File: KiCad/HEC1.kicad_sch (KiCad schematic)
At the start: 39 parts, among them J1 Barrel_Jack_Switch, J5 Screw_Terminal_01x02, U41 74LS02

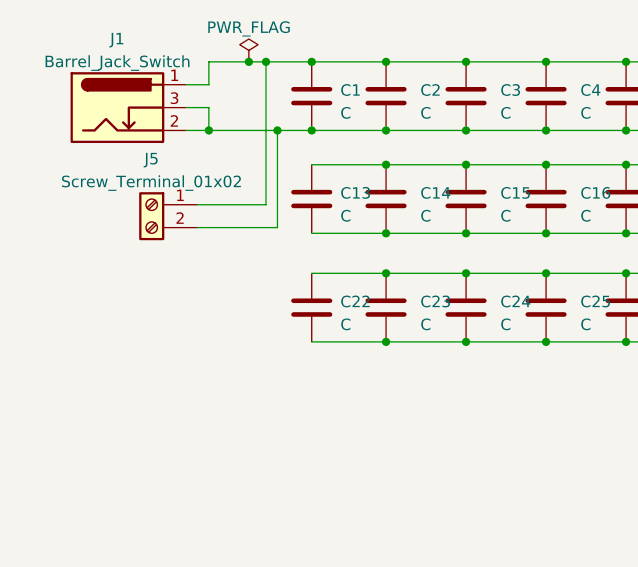
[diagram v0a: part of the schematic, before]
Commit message: More routing, a power LED
Did some easier routing. The current concern is that the already done easy routing would take up space for harder to route traces, making them even harder. However, one have to start somewhere... The power LED is added to assist debugging.
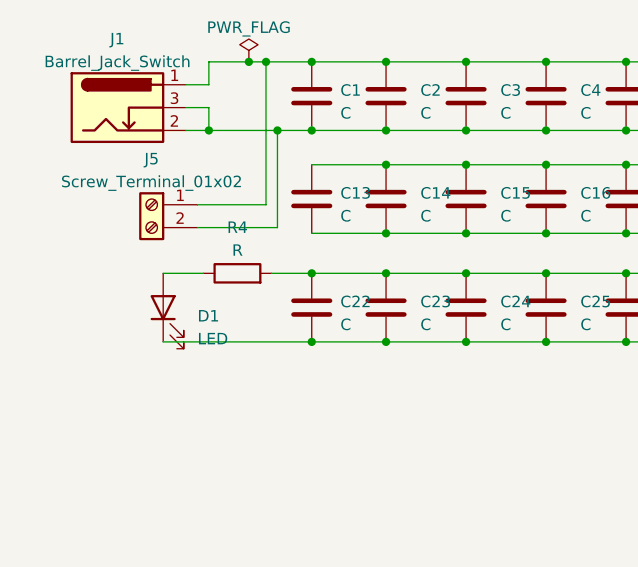
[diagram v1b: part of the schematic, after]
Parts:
- added D1: LED, LED_THT:LED_D3.0mm, symbol Device:LED
- added R4: R, Resistor_THT:R_Axial_DIN0207_L6.3mm_D2.5mm_P7.62mm_Horizontal, symbol Device:R
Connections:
- net GND: now also D1.1 (K)
- net VCC: now also R4.2
- new net: D1.2 (A), R4.1
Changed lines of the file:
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@@
   (junction (at 118.11 55.88) (diameter 0) (color 0 0 0 0)
   )
+  (junction (at 73.66 143.51) (diameter 0) (color 0 0 0 0)
+  )
   (junction (at 90.805 143.51) (diameter 0) (color 0 0 0 0)
   )
@@
   )
   (junction (at 177.165 28.575) (diameter 0) (color 0 0 0 0)
+  )
+  (junction (at 73.66 135.89) (diameter 0) (color 0 0 0 0)
   )
   (junction (at 68.58 112.395) (diameter 0) (color 0 0 0 0)
@@
     (stroke (width 0) (type default))
   )
+  (wire (pts (xy 57.15 135.89) (xy 61.595 135.89))
+    (stroke (width 0) (type default))
+  )
   (wire (pts (xy 133.985 60.96) (xy 133.985 43.815))
     (stroke (width 0) (type default))
@@
     (stroke (width 0) (type default))
   )
+  (wire (pts (xy 69.215 135.89) (xy 73.66 135.89))
+    (stroke (width 0) (type default))
+  )
   (wire (pts (xy 191.135 112.395) (xy 199.39 112.395))
     (stroke (width 0) (type default))
@@
   )
   (bus (pts (xy 113.03 83.185) (xy 118.11 83.185))
+    (stroke (width 0) (type default))
+  )
+  (wire (pts (xy 57.15 143.51) (xy 73.66 143.51))
     (stroke (width 0) (type default))
   )
@@
         (path "/87935374-b60a-4f41-99da-94b76103dd77"
           (reference "C27") (unit 1)
+        )
+      )
+    )
+  )
+  (symbol (lib_id "Device:LED") (at 57.15 139.7 90) (unit 1)
+    (in_bom yes) (on_board yes) (dnp no) (fields_autoplaced)
+    (property "Reference" "D1" (at 60.96 140.6525 90)
+      (effects (font (size 1.27 1.27)) (justify right))
+    )
+    (property "Value" "LED" (at 60.96 143.1925 90)
+      (effects (font (size 1.27 1.27)) (justify right))
+    )
+    (property "Footprint" "LED_THT:LED_D3.0mm" (at 57.15 139.7 0)
+      (effects (font (size 1.27 1.27)) hide)
+    )
+    (property "Datasheet" "~" (at 57.15 139.7 0)
+      (effects (font (size 1.27 1.27)) hide)
+    )
+    (pin "1")
+    (pin "2")
+    (instances
+      (project "HEC1"
+        (path "/87935374-b60a-4f41-99da-94b76103dd77"
+          (reference "D1") (unit 1)
         )
       )
@@
         )
       )
+    )
+  )
+  (symbol (lib_id "Device:R") (at 65.405 135.89 90) (unit 1)
+    (in_bom yes) (on_board yes) (dnp no) (fields_autoplaced)
+    (property "Reference" "R4" (at 65.405 130.81 90)
+      (effects (font (size 1.27 1.27)))
+    )
+    (property "Value" "R" (at 65.405 133.35 90)
+      (effects (font (size 1.27 1.27)))
+    )
+    (property "Footprint" "Resistor_THT:R_Axial_DIN0207_L6.3mm_D2.5mm_P7.62mm_Horizontal" (at 65.405 137.668 90)
+      (effects (font (size 1.27 1.27)) hide)
+    )
+    (property "Datasheet" "~" (at 65.405 135.89 0)
+      (effects (font (size 1.27 1.27)) hide)
+    )
+    (pin "1")
+    (pin "2")
+    (instances
+      (project "HEC1"
+        (path "/87935374-b60a-4f41-99da-94b76103dd77"
+          (reference "R4") (unit 1)
+        )
+      )

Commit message: Livestream commit
Committing live! Just to make sure that I don't lose 1 day of work.
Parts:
- removed unit 4 of U41
- removed unit 3 of U41
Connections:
- no-connect marks 3 -> 1

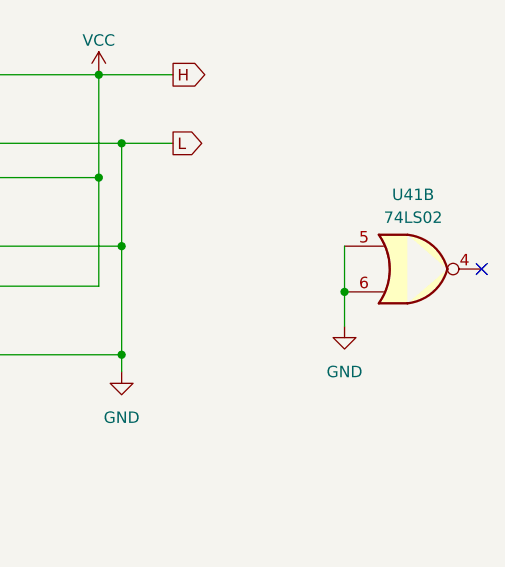
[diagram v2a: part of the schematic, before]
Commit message: Finish routing data bus
finished routing arguably the hardest part of the board: the data bus. The routing is mostly complete. However, the rest of traces are very hard to route. One more day of work is expected.
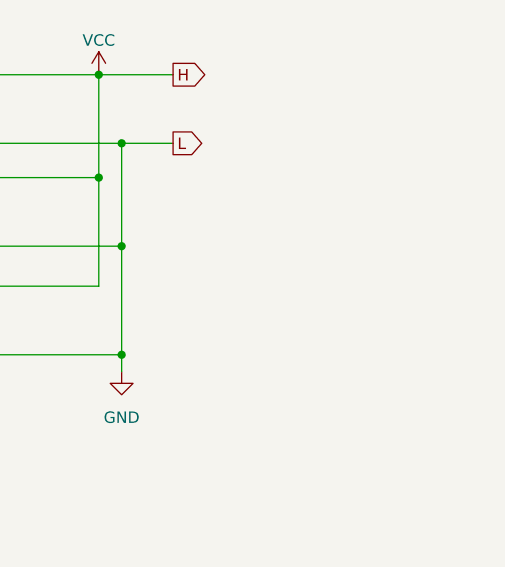
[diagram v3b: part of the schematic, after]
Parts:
- removed U41: 74LS02, Package_DIP:DIP-14_W7.62mm_Socket, symbol 74xx:74LS02
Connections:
- no-connect marks 1 -> 0
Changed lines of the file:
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@@
   (junction (at 193.675 120.015) (diameter 0) (color 0 0 0 0)
   )
-  (junction (at 218.44 136.525) (diameter 0) (color 0 0 0 0)
-  )
   (junction (at 144.145 123.825) (diameter 0) (color 0 0 0 0)
   )
@@
   (junction (at 161.29 120.015) (diameter 0) (color 0 0 0 0)
   )
-  (no_connect (at 233.68 133.985))
   (wire (pts (xy 90.805 112.395) (xy 99.695 112.395))
     (stroke (width 0) (type default))
@@
     (stroke (width 0) (type default))
   )
-  (wire (pts (xy 218.44 131.445) (xy 218.44 136.525))
-    (stroke (width 0) (type default))
-  )
   (wire (pts (xy 133.985 43.815) (xy 135.89 43.815))
     (stroke (width 0) (type default))
@@
   )
   (wire (pts (xy 144.145 131.445) (xy 161.29 131.445))
-    (stroke (width 0) (type default))
-  )
-  (wire (pts (xy 218.44 136.525) (xy 218.44 140.335))
     (stroke (width 0) (type default))
   )
@@
     )
   )
-  (symbol (lib_id "power:GND") (at 218.44 140.335 0) (unit 1)
-    (in_bom yes) (on_board yes) (dnp no) (fields_autoplaced)
-    (property "Reference" "#PWR0106" (at 218.44 146.685 0)
-      (effects (font (size 1.27 1.27)) hide)
-    )
-    (property "Value" "GND" (at 218.44 145.415 0)
-      (effects (font (size 1.27 1.27)))
-    )
-    (property "Footprint" "" (at 218.44 140.335 0)
-      (effects (font (size 1.27 1.27)) hide)
-    )
-    (property "Datasheet" "" (at 218.44 140.335 0)
-      (effects (font (size 1.27 1.27)) hide)
-    )
-    (pin "1")
-    (instances
-      (project "HEC1"
-        (path "/87935374-b60a-4f41-99da-94b76103dd77"
-          (reference "#PWR0106") (unit 1)
-        )
-      )
-    )
-  )
   (symbol (lib_id "power:GND") (at 193.675 145.415 0) (unit 1)
     (in_bom yes) (on_board yes) (dnp no) (fields_autoplaced)
@@
         )
       )
-    )
-  )
-  (symbol (lib_id "74xx:74LS02") (at 226.06 133.985 0) (unit 2)
-    (in_bom yes) (on_board yes) (dnp no) (fields_autoplaced)
-    (property "Reference" "U41" (at 226.06 125.73 0)
-      (effects (font (size 1.27 1.27)))
-    )
-    (property "Value" "74LS02" (at 226.06 128.27 0)
-      (effects (font (size 1.27 1.27)))
-    )
-    (property "Footprint" "Package_DIP:DIP-14_W7.62mm_Socket" (at 226.06 133.985 0)
-      (effects (font (size 1.27 1.27)) hide)
-    )
-    (property "Datasheet" "http://www.ti.com/lit/gpn/sn74ls02" (at 226.06 133.985 0)
-      (effects (font (size 1.27 1.27)) hide)
-    )
-    (pin "1")
-    (pin "2")
-    (pin "3")
-    (pin "4")
-    (pin "5")
-    (pin "6")
-    (pin "10")
-    (pin "8")
-    (pin "9")
-    (pin "11")
-    (pin "12")
-    (pin "13")
-    (pin "14")
-    (pin "7")
-    (instances
-      (project "HEC1"
-        (path "/87935374-b60a-4f41-99da-94b76103dd77/2930b625-d6a3-4a7f-9d41-a454efcef99d"
-          (reference "U41") (unit 2)
-        )
-        (path "/87935374-b60a-4f41-99da-94b76103dd77"
-          (reference "U41") (unit 2)
-        )
-      )

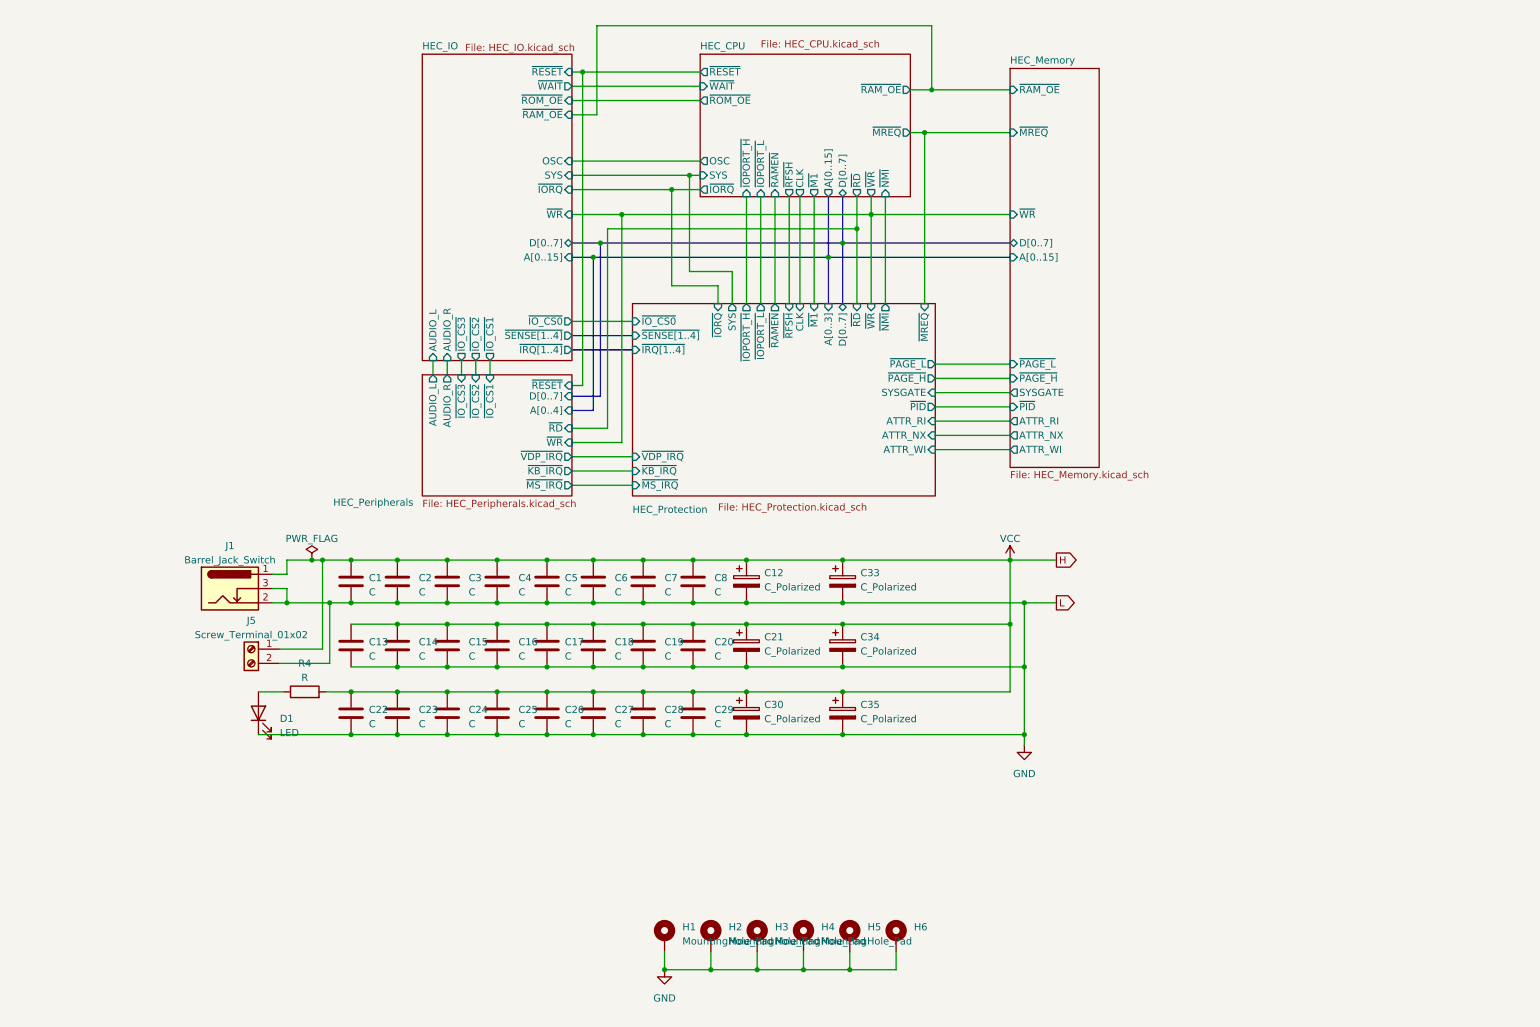
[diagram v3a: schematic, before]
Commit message: Change LED display type
Changed LED display to include two decimal points to indicate usr/sys mode. This type of LED display is easier to source.
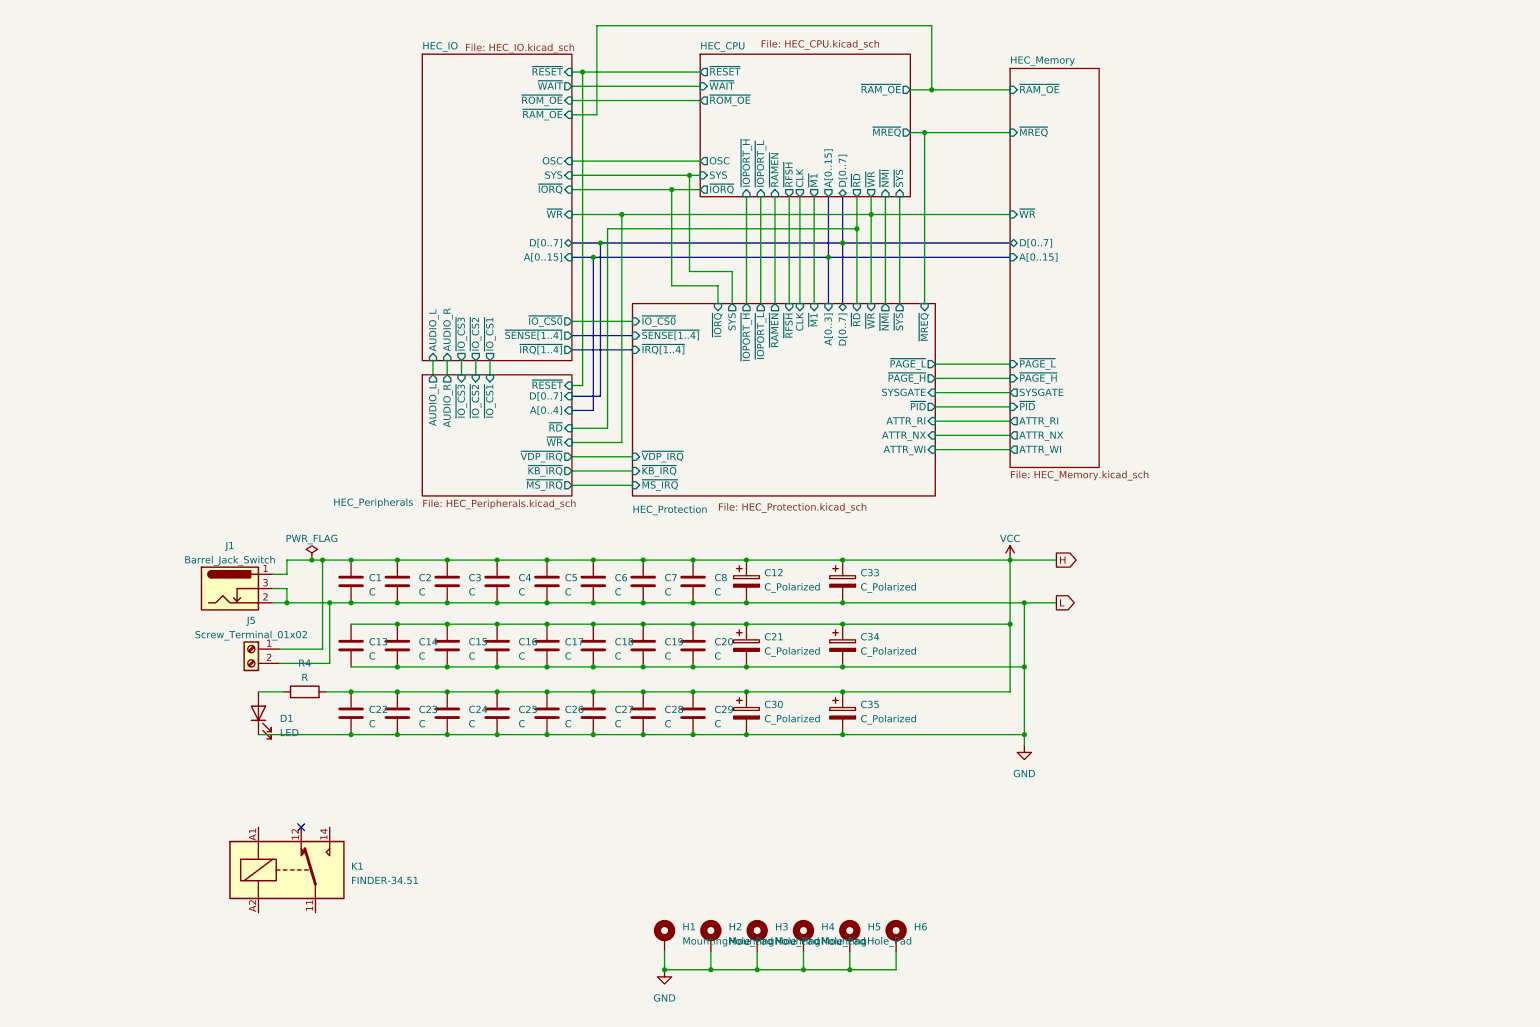
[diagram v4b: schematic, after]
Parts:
- added K1: FINDER-34.51, Relay_THT:Relay_SPDT_Finder_34.51_Vertical, symbol Relay:FINDER-34.51
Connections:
- no-connect marks 0 -> 1
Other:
- sheet HEC_CPU ports: added ~{SYS}; removed none
- sheet HEC_Protection ports: added ~{SYS}; removed none
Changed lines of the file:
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@@
   (junction (at 161.29 120.015) (diameter 0) (color 0 0 0 0)
   )
+  (no_connect (at 64.77 160.02))
   (wire (pts (xy 90.805 112.395) (xy 99.695 112.395))
     (stroke (width 0) (type default))
@@
   )
   (wire (pts (xy 144.145 131.445) (xy 161.29 131.445))
+    (stroke (width 0) (type default))
+  )
+  (wire (pts (xy 171.45 47.625) (xy 171.45 66.675))
     (stroke (width 0) (type default))
   )
@@
         (path "/87935374-b60a-4f41-99da-94b76103dd77"
           (reference "C34") (unit 1)
+        )
+      )
+    )
+  )
+  (symbol (lib_id "Relay:FINDER-34.51") (at 62.23 167.64 0) (unit 1)
+    (in_bom yes) (on_board yes) (dnp no) (fields_autoplaced)
+    (property "Reference" "K1" (at 73.66 167.005 0)
+      (effects (font (size 1.27 1.27)) (justify left))
+    )
+    (property "Value" "FINDER-34.51" (at 73.66 169.545 0)
+      (effects (font (size 1.27 1.27)) (justify left))
+    )
+    (property "Footprint" "Relay_THT:Relay_SPDT_Finder_34.51_Vertical" (at 91.186 168.656 0)
+      (effects (font (size 1.27 1.27)) hide)
+    )
+    (property "Datasheet" "https://gfinder.findernet.com/public/attachments/34/EN/S34USAEN.pdf" (at 62.23 167.64 0)
+      (effects (font (size 1.27 1.27)) hide)
+    )
+    (pin "11")
+    (pin "12")
+    (pin "14")
+    (pin "A1")
+    (pin "A2")
+    (instances
+      (project "HEC1"
+        (path "/87935374-b60a-4f41-99da-94b76103dd77"
+          (reference "K1") (unit 1)
         )
       )
@@
       (effects (font (size 1.27 1.27)) (justify right))
     )
+    (pin "~{SYS}" output (at 171.45 66.675 90)
+      (effects (font (size 1.27 1.27)) (justify right))
+    )
     (instances
       (project "HEC1"
@@
       (effects (font (size 1.27 1.27)) (justify left))
     )
+    (pin "~{SYS}" input (at 171.45 47.625 270)
+      (effects (font (size 1.27 1.27)) (justify left))
+    )

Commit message: change NX bit to XE bit
change No eXecute to eXecute Enable (inverting the polarity of the signal) in order to fix a bug that causes the HEC to not recognize a NX when the instruction fetched is a RST.
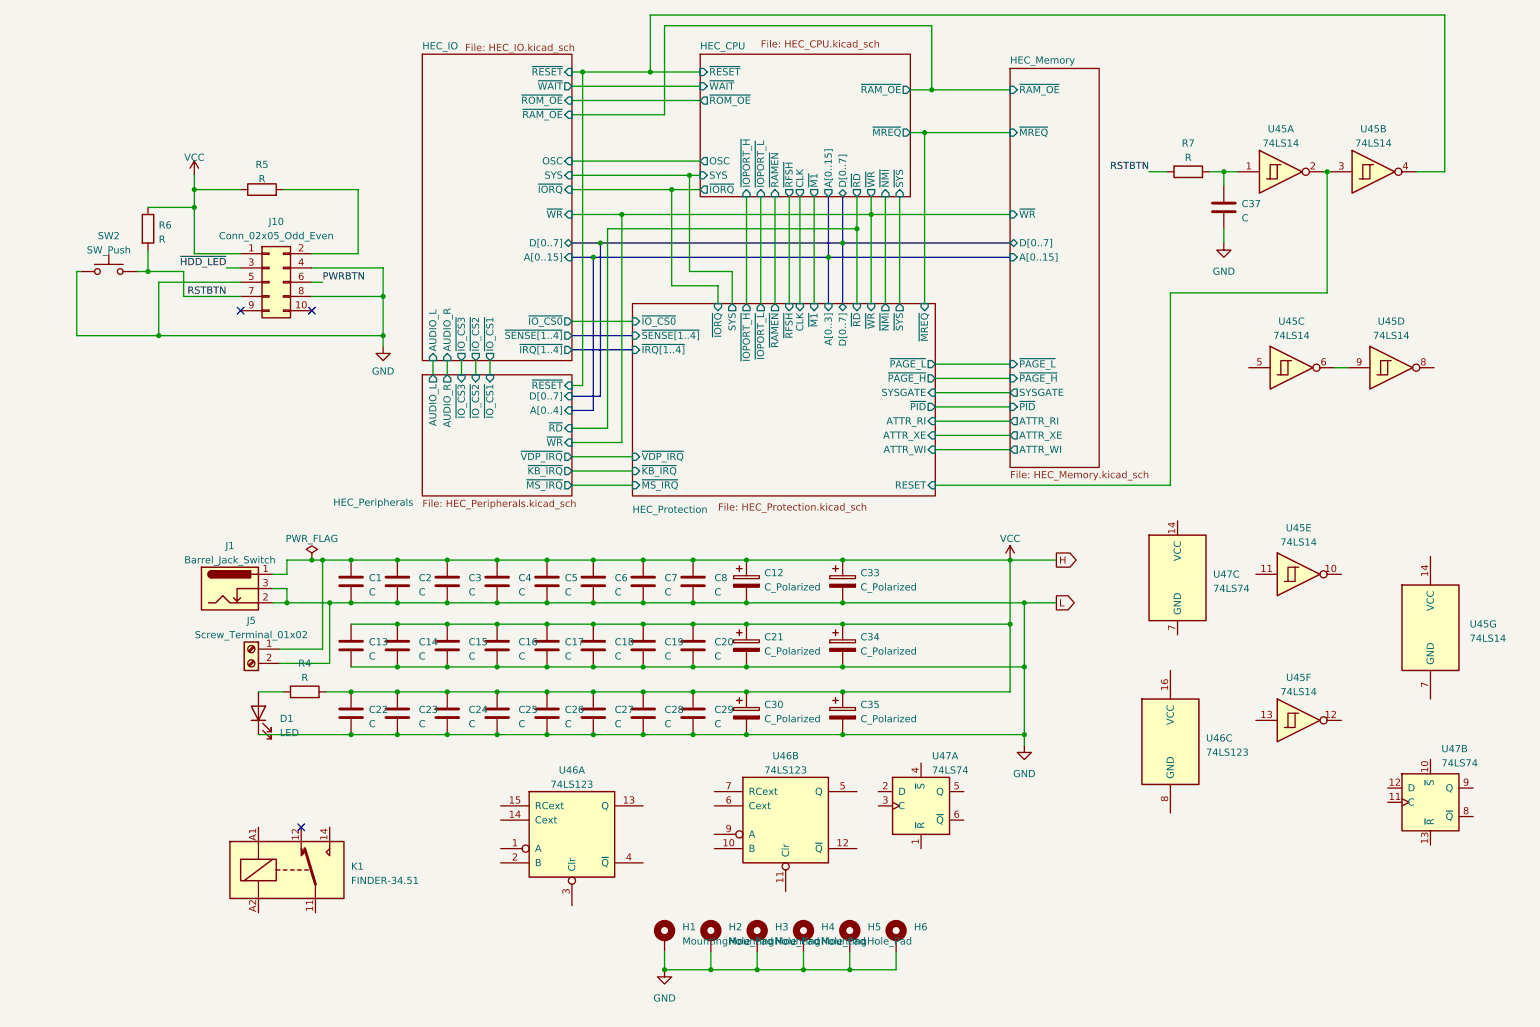
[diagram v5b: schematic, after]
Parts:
- added C37: C, symbol Device:C
- added J10: Conn_02x05_Odd_Even, symbol Connector_Generic:Conn_02x05_Odd_Even
- added R5, R6, R7: R, symbol Device:R
- added SW2: SW_Push, Button_Switch_THT:SW_PUSH_6mm, symbol Switch:SW_Push
- added U45: 74LS14, symbol 74xx:74LS14
- added U46: 74LS123, symbol 74xx:74LS123
- added U47: 74LS74, symbol 74xx:74LS74
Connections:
- net GND: now also C37.2, J10.4 (Pin_4), J10.5 (Pin_5), J10.8 (Pin_8), SW2.2
- net HEC_CPU/~{RESET}: now also U45.4
- net VCC: now also J10.1 (Pin_1), R5.1, R6.1
- new net: J10.2 (Pin_2), R5.2
- new net: C37.1, R7.2, U45.1
- new net: U45.6, U45.9
- new net HEC_Protection/RESET: U45.2, U45.3
- new net PWRBTN: J10.6 (Pin_6)
- new net RSTBTN: J10.7 (Pin_7), R6.2, R7.1, SW2.1
- new net ~{HDD_LED}: J10.3 (Pin_3)
- no-connect marks 1 -> 3
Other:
- sheet HEC_Memory ports: added ATTR_XE; removed ATTR_NX
- sheet HEC_Protection ports: added ATTR_XE, RESET; removed ATTR_NX
